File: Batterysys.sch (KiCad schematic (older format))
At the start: 160 parts

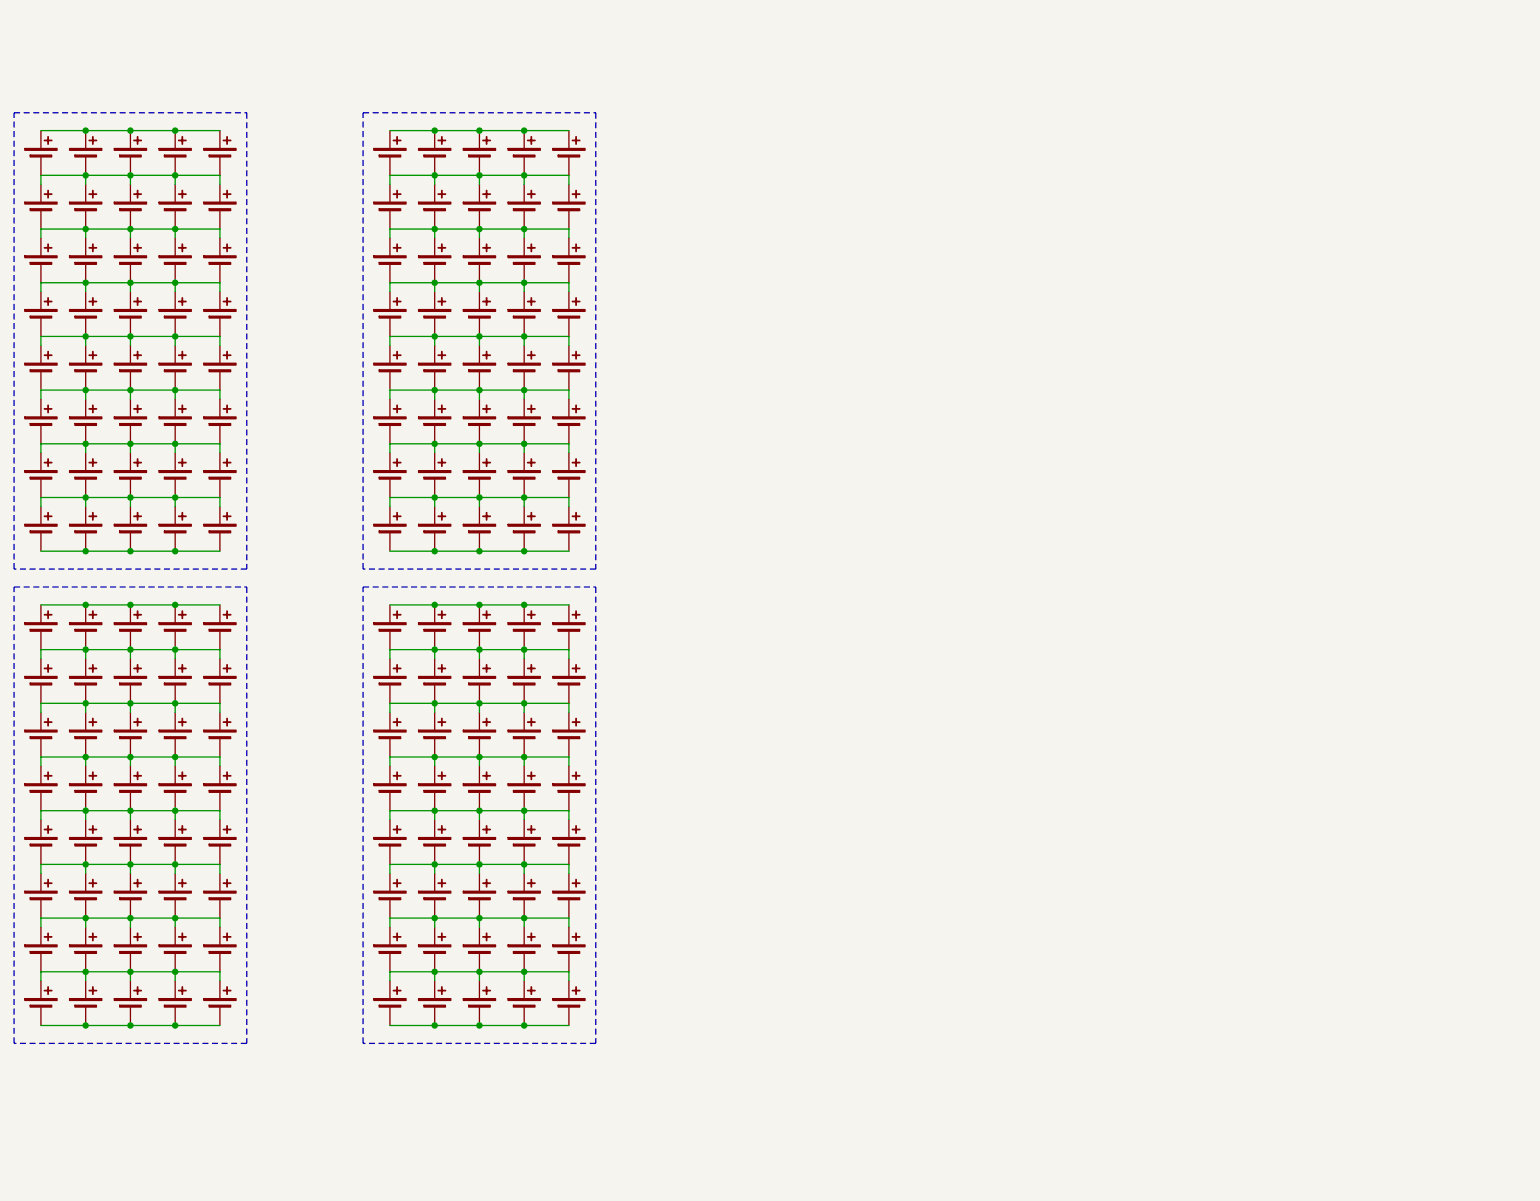
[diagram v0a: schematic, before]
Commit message: Changed Display, finished cell array, added CAN bus
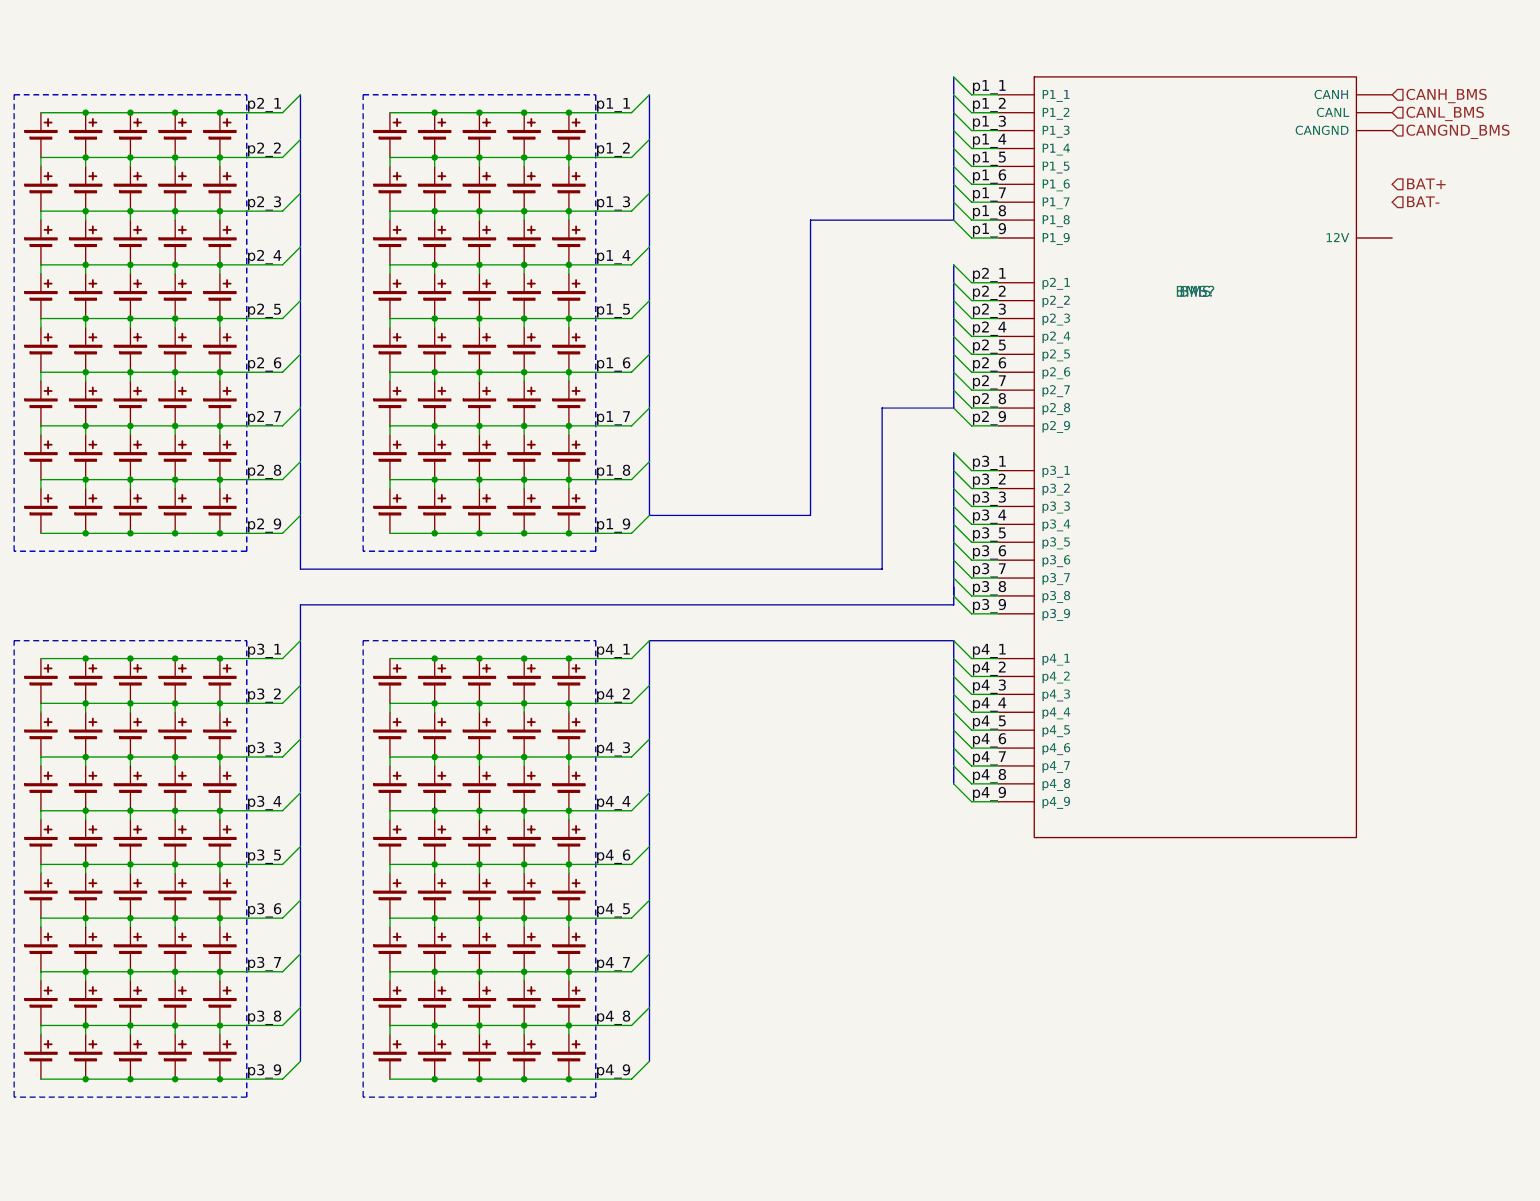
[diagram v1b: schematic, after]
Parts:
- added BMS?: BMS, symbol BMS
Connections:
- net p2_1: now reaches CELL?.1, CELL?.1, CELL?.1, CELL?.1, CELL?.1
- net p2_1: now also BMS?.~ (p4_9)
- net p2_2: now reaches CELL?.1, CELL?.1, CELL?.1, CELL?.1, CELL?.1, CELL?.2, CELL?.2, CELL?.2, CELL?.2, CELL?.2
- net p2_2: now also BMS?.~ (p4_9)
- net p2_3: now reaches CELL?.1, CELL?.1, CELL?.1, CELL?.1, CELL?.1, CELL?.2, CELL?.2, CELL?.2, CELL?.2, CELL?.2
- net p2_3: now also BMS?.~ (p4_9)
- net p2_4: now reaches CELL?.1, CELL?.1, CELL?.1, CELL?.1, CELL?.1, CELL?.2, CELL?.2, CELL?.2, CELL?.2, CELL?.2
- net p2_4: now also BMS?.~ (p4_9)
- net p2_5: now reaches CELL?.1, CELL?.1, CELL?.1, CELL?.1, CELL?.1, CELL?.2, CELL?.2, CELL?.2, CELL?.2, CELL?.2
- net p2_5: now also BMS?.~ (p4_9)
- net p2_6: now reaches CELL?.1, CELL?.1, CELL?.1, CELL?.1, CELL?.1, CELL?.2, CELL?.2, CELL?.2, CELL?.2, CELL?.2
- net p2_6: now also BMS?.~ (p4_9)
- net p2_7: now reaches CELL?.1, CELL?.1, CELL?.1, CELL?.1, CELL?.1, CELL?.2, CELL?.2, CELL?.2, CELL?.2, CELL?.2
- net p2_7: now also BMS?.~ (p4_9)
- net p2_8: now reaches CELL?.1, CELL?.1, CELL?.1, CELL?.1, CELL?.1, CELL?.2, CELL?.2, CELL?.2, CELL?.2, CELL?.2
- net p2_8: now also BMS?.~ (p4_9)
- net p2_9: now reaches CELL?.2, CELL?.2, CELL?.2, CELL?.2, CELL?.2
- net p2_9: now also BMS?.~ (p4_9)
- net p3_1: now reaches CELL?.1, CELL?.1, CELL?.1, CELL?.1, CELL?.1
- net p3_1: now also BMS?.~ (p4_9)
- net p3_2: now reaches CELL?.1, CELL?.1, CELL?.1, CELL?.1, CELL?.1, CELL?.2, CELL?.2, CELL?.2, CELL?.2, CELL?.2
- net p3_2: now also BMS?.~ (p4_9)
- net p3_3: now reaches CELL?.1, CELL?.1, CELL?.1, CELL?.1, CELL?.1, CELL?.2, CELL?.2, CELL?.2, CELL?.2, CELL?.2
- net p3_3: now also BMS?.~ (p4_9)
- net p3_4: now reaches CELL?.1, CELL?.1, CELL?.1, CELL?.1, CELL?.1, CELL?.2, CELL?.2, CELL?.2, CELL?.2, CELL?.2
- net p3_4: now also BMS?.~ (p4_9)
- net p3_5: now reaches CELL?.1, CELL?.1, CELL?.1, CELL?.1, CELL?.1, CELL?.2, CELL?.2, CELL?.2, CELL?.2, CELL?.2
- net p3_5: now also BMS?.~ (p4_9)
- net p3_6: now reaches CELL?.1, CELL?.1, CELL?.1, CELL?.1, CELL?.1, CELL?.2, CELL?.2, CELL?.2, CELL?.2, CELL?.2
- net p3_6: now also BMS?.~ (p4_9)
- net p3_7: now reaches CELL?.1, CELL?.1, CELL?.1, CELL?.1, CELL?.1, CELL?.2, CELL?.2, CELL?.2, CELL?.2, CELL?.2
- net p3_7: now also BMS?.~ (p4_9)
- net p3_8: now reaches CELL?.1, CELL?.1, CELL?.1, CELL?.1, CELL?.1, CELL?.2, CELL?.2, CELL?.2, CELL?.2, CELL?.2
- net p3_8: now also BMS?.~ (p4_9)
- net p3_9: now reaches CELL?.2, CELL?.2, CELL?.2, CELL?.2, CELL?.2
- net p3_9: now also BMS?.~ (p4_9)
- net p1_1: now reaches CELL?.1, CELL?.1, CELL?.1, CELL?.1, CELL?.1
- net p1_1: now also BMS?.~ (p4_9)
- net p1_2: now reaches CELL?.1, CELL?.1, CELL?.1, CELL?.1, CELL?.1, CELL?.2, CELL?.2, CELL?.2, CELL?.2, CELL?.2
- net p1_2: now also BMS?.~ (p4_9)
- net p1_3: now reaches CELL?.1, CELL?.1, CELL?.1, CELL?.1, CELL?.1, CELL?.2, CELL?.2, CELL?.2, CELL?.2, CELL?.2
- net p1_3: now also BMS?.~ (p4_9)
- net p1_4: now reaches CELL?.1, CELL?.1, CELL?.1, CELL?.1, CELL?.1, CELL?.2, CELL?.2, CELL?.2, CELL?.2, CELL?.2
- net p1_4: now also BMS?.~ (p4_9)
- net p1_5: now reaches CELL?.1, CELL?.1, CELL?.1, CELL?.1, CELL?.1, CELL?.2, CELL?.2, CELL?.2, CELL?.2, CELL?.2
- net p1_5: now also BMS?.~ (p4_9)
- net p1_6: now reaches CELL?.1, CELL?.1, CELL?.1, CELL?.1, CELL?.1, CELL?.2, CELL?.2, CELL?.2, CELL?.2, CELL?.2
- net p1_6: now also BMS?.~ (p4_9)
- net p1_7: now reaches CELL?.1, CELL?.1, CELL?.1, CELL?.1, CELL?.1, CELL?.2, CELL?.2, CELL?.2, CELL?.2, CELL?.2
- net p1_7: now also BMS?.~ (p4_9)
- net p1_8: now reaches CELL?.1, CELL?.1, CELL?.1, CELL?.1, CELL?.1, CELL?.2, CELL?.2, CELL?.2, CELL?.2, CELL?.2
- net p1_8: now also BMS?.~ (p4_9)
- net p1_9: now reaches CELL?.2, CELL?.2, CELL?.2, CELL?.2, CELL?.2
- net p1_9: now also BMS?.~ (p4_9)
- net p4_1: now reaches CELL?.1, CELL?.1, CELL?.1, CELL?.1, CELL?.1
- net p4_1: now also BMS?.~ (p4_9)
- net p4_2: now reaches CELL?.1, CELL?.1, CELL?.1, CELL?.1, CELL?.1, CELL?.2, CELL?.2, CELL?.2, CELL?.2, CELL?.2
- net p4_2: now also BMS?.~ (p4_9)
- net p4_3: now reaches CELL?.1, CELL?.1, CELL?.1, CELL?.1, CELL?.1, CELL?.2, CELL?.2, CELL?.2, CELL?.2, CELL?.2
- net p4_3: now also BMS?.~ (p4_9)
- net p4_4: now reaches CELL?.1, CELL?.1, CELL?.1, CELL?.1, CELL?.1, CELL?.2, CELL?.2, CELL?.2, CELL?.2, CELL?.2
- net p4_4: now also BMS?.~ (p4_9)
- net p4_6: now reaches CELL?.1, CELL?.1, CELL?.1, CELL?.1, CELL?.1, CELL?.2, CELL?.2, CELL?.2, CELL?.2, CELL?.2
- net p4_6: now also BMS?.~ (p4_9)
- net p4_5: now reaches CELL?.1, CELL?.1, CELL?.1, CELL?.1, CELL?.1, CELL?.2, CELL?.2, CELL?.2, CELL?.2, CELL?.2
- net p4_5: now also BMS?.~ (p4_9)
- net p4_7: now reaches CELL?.1, CELL?.1, CELL?.1, CELL?.1, CELL?.1, CELL?.2, CELL?.2, CELL?.2, CELL?.2, CELL?.2
- net p4_7: now also BMS?.~ (p4_9)
- net p4_8: now reaches CELL?.1, CELL?.1, CELL?.1, CELL?.1, CELL?.1, CELL?.2, CELL?.2, CELL?.2, CELL?.2, CELL?.2
- net p4_8: now also BMS?.~ (p4_9)
- net p4_9: now reaches CELL?.2, CELL?.2, CELL?.2, CELL?.2, CELL?.2
- net p4_9: now also BMS?.~ (p4_9)
- new net CANGND_BMS: BMS?.~ (p4_9)
- new net CANH_BMS: BMS?.~ (p4_9)
- new net CANL_BMS: BMS?.~ (p4_9)

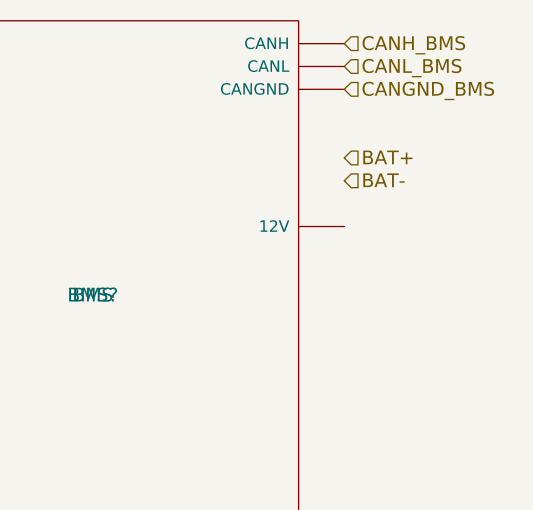
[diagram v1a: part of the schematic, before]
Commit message: Emergency switches and ignition/precharge leds
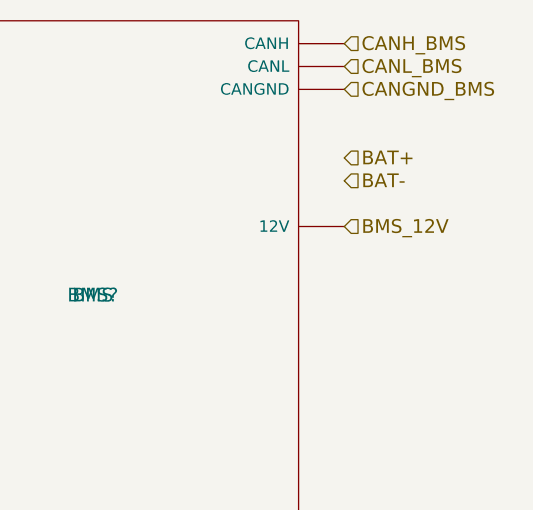
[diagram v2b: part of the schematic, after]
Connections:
- new net BMS_12V: BMS?.~ (p4_9)
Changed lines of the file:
@@
 Text HLabel 9800 1950 2    60   Input ~ 0
 BAT-
+Text HLabel 9800 2150 2    60   Input ~ 0
+BMS_12V
 $EndSCHEMATC

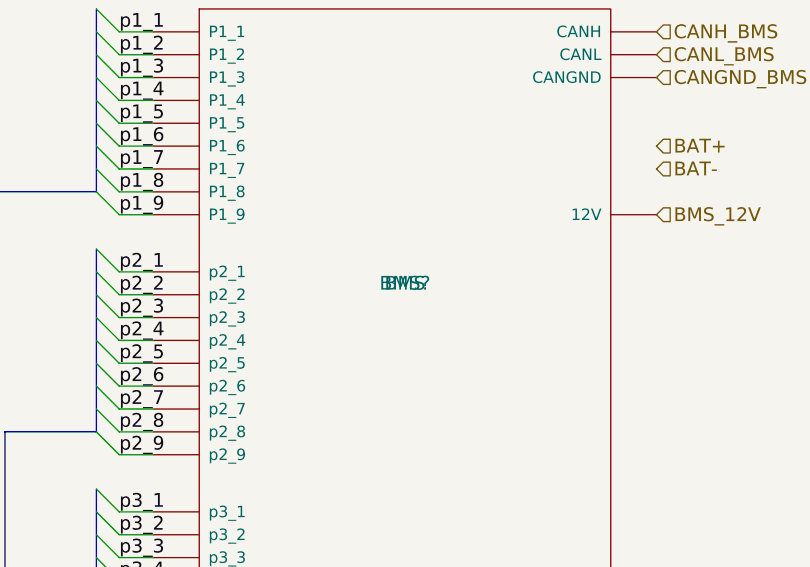
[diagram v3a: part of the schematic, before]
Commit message: Changed a few labels
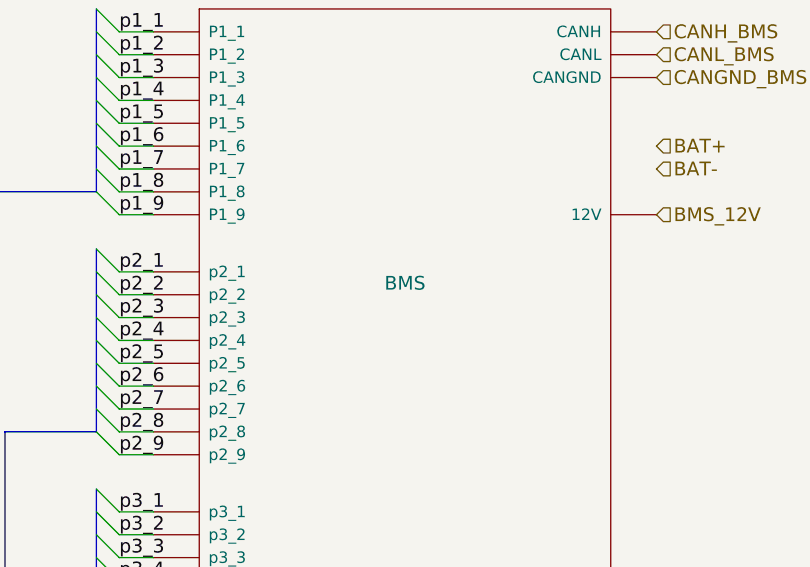
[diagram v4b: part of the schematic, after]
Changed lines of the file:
@@
 U 1 1 56C89866
 P 8700 2450
-F 0 "BMS?" H 8700 2450 60  0000 C CNN
+F 0 "BMS?" H 8700 2450 60  0001 C CNN
 F 1 "BMS" H 8700 2450 60  0000 C CNN
 F 2 "" H 8700 2450 60  0000 C CNN

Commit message: Fixed up a few things
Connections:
- net BAT+: now also BMS?.~ (p4_9), CELL?.1, CELL?.1, CELL?.1, CELL?.1, CELL?.1
- net BAT-: now also BMS?.~ (p4_9), CELL?.2, CELL?.2, CELL?.2, CELL?.2, CELL?.2
- net p1_9: now also CELL?.1, CELL?.1, CELL?.1, CELL?.1, CELL?.1
- net p2_1: now also CELL?.2, CELL?.2, CELL?.2, CELL?.2, CELL?.2
- net p2_9: now also CELL?.1, CELL?.1, CELL?.1, CELL?.1, CELL?.1
- removed net p1_1: BMS?.~ (p4_9), CELL?.1, CELL?.1, CELL?.1, CELL?.1, CELL?.1
- removed net p3_1: BMS?.~ (p4_9), CELL?.1, CELL?.1, CELL?.1, CELL?.1, CELL?.1
- removed net p3_9: BMS?.~ (p4_9), CELL?.2, CELL?.2, CELL?.2, CELL?.2, CELL?.2
- removed net p4_1: BMS?.~ (p4_9), CELL?.1, CELL?.1, CELL?.1, CELL?.1, CELL?.1
- removed net p4_9: BMS?.~ (p4_9), CELL?.2, CELL?.2, CELL?.2, CELL?.2, CELL?.2
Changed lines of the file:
@@
 Text HLabel 9800 1550 2    60   Input ~ 0
 CANGND_BMS
-Text HLabel 9800 1850 2    60   Input ~ 0
+Text HLabel 4700 1250 1    60   Input ~ 0
 BAT+
-Text HLabel 9800 1950 2    60   Input ~ 0
+Text HLabel 2750 7100 3    60   Input ~ 0
 BAT-
 Text HLabel 9800 2150 2    60   Input ~ 0
 BMS_12V
+Wire Wire Line
+	2750 3800 2750 4500
+Wire Wire Line
+	2750 6850 2750 7100
+Wire Wire Line
+	4700 7100 4700 6850
+Wire Wire Line
+	4700 4500 4700 3800
+Wire Wire Line
+	4700 1450 4700 1250
+Wire Wire Line
+	2750 1450 2750 1250
+Wire Wire Line
+	2750 1250 3900 1250
+Wire Wire Line
+	3900 1250 3900 7100
+Wire Wire Line
+	3900 7100 4700 7100
 $EndSCHEMATC
